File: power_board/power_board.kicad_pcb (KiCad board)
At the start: 2 copper layers, 165.3 x 119.6 mm, 78 parts, among them J1 PROG, J10 M4, J11 5V_1, J12 M5, J13 M6, J14 M7, J15 FAN, J16 Screw_Terminal_01x02, J17 MB_interface, J18 Conn_01x02_Female, J19 12V_1, J2 M1, J20 12V_2, J21 12V_3, J22 12V_4, J23 48V_1, J24 48V_2, J25 48V_3, J26 48V_4, J27 Screw_Terminal_01x02, J3 M2, J4 Conn_01x02_Female, J5 Conn_01x02_Female, J6 Conn_01x01_Male, J7 Conn_01x01_Male, J8 Screw_Terminal_01x02, J9 M3, Q1 2N3906, SW1 SW_Push, U1 ACS758xCB-050B-PFF, U10 MAX31855KASA, U2 ACS758xCB-050B-PFF, U3 MCP2515-EST, U4 MAX31855KASA, U5 MCP2551-I-SN, U6 BTS50085-1TMA, U7 ATmega328P-AU, U8 BTS50085-1TMA, U9 LM2596S-5, Y1 20Mhz, Y2 16Mhz

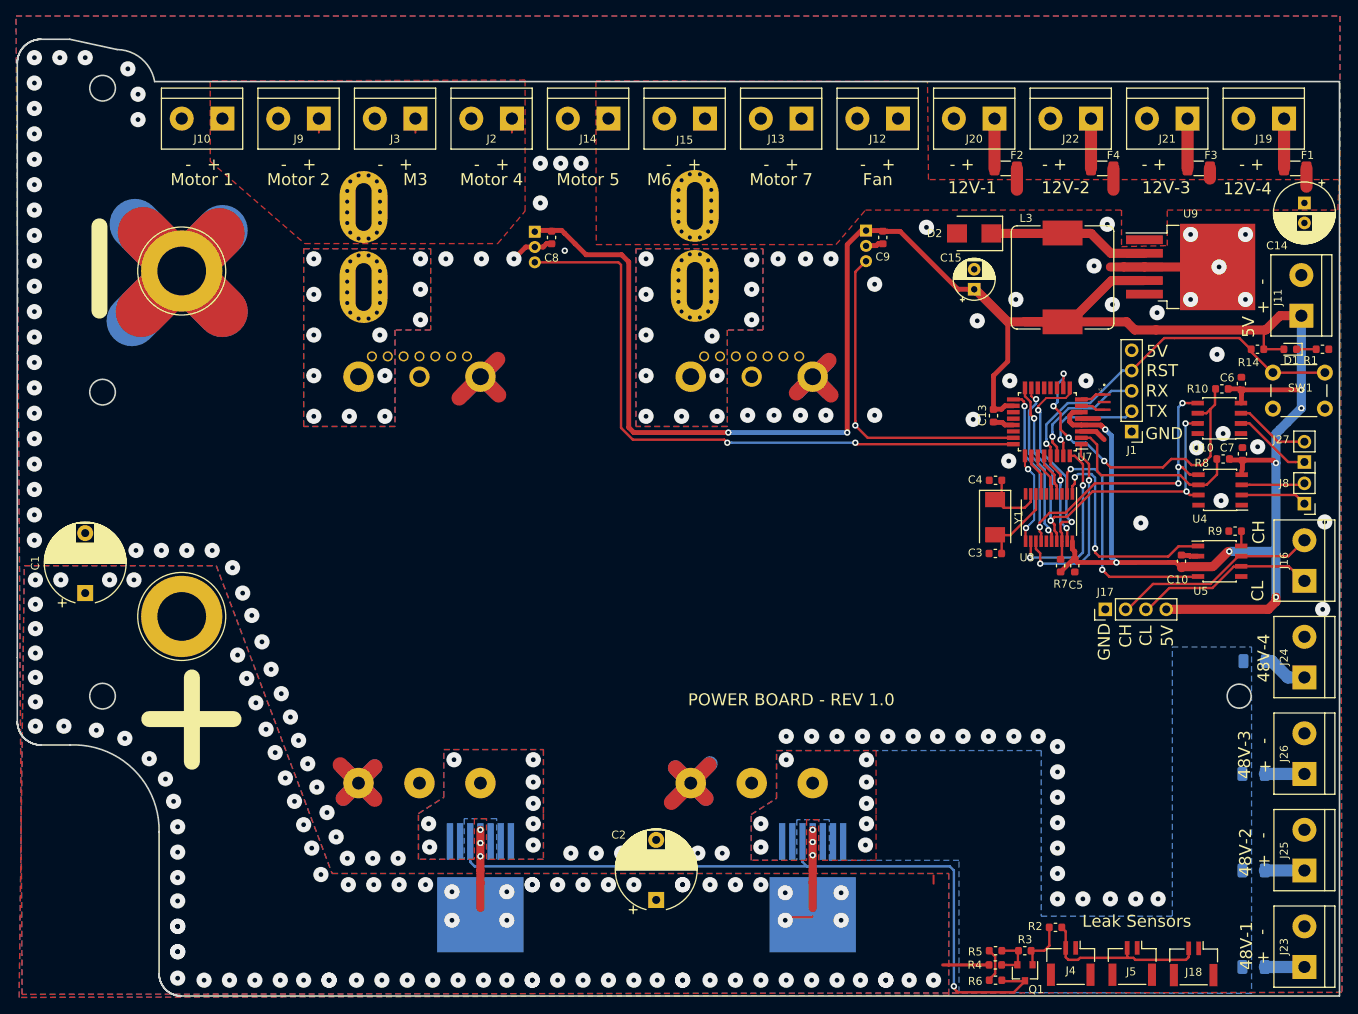
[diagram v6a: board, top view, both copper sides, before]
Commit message: finished re-routing for v_prog diode
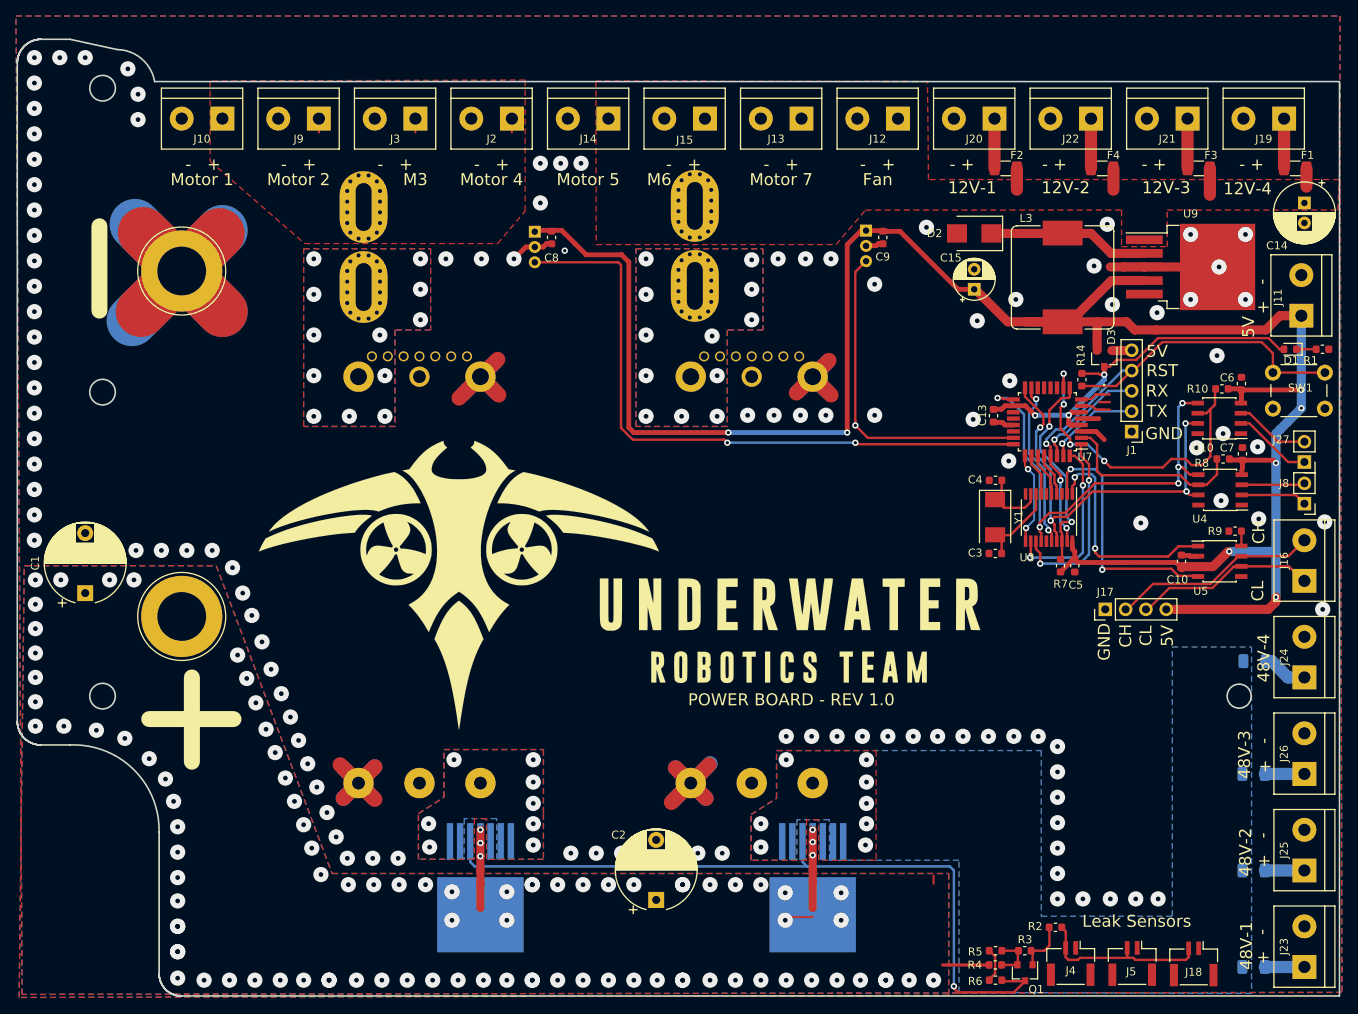
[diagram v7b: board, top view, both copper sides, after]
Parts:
- added D3: D_x2_KCom_AAK, Package_TO_SOT_SMD:SOT-23, F.Cu at (196.6, 71.9)
- added G***: LOGO, logo:logo, F.Cu at (116.1, 99.9)
- added G***: LOGO, title:title, F.Cu at (157.1, 106.2)
- moved R14 22.3 mm to (193.8, 74.5), turned to 270 degrees
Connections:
- C13 pad 1: +5V -> V_MCU
- D1 pad 2: +5V -> V_MCU
- J1 pad 5: +5V -> VPP
- R14 pad 1: +5V -> V_MCU
- U7 pad 18: +5V -> V_MCU
- U7 pad 4: +5V -> V_MCU
- U7 pad 6: +5V -> V_MCU
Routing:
- net V_MCU: track 0.00 -> 49.7 mm, vias 0 -> 3
- net +5V: track 311.0 -> 271.4 mm, vias 9 -> 7
- net RESET: track 57.1 -> 64.0 mm
- net SCK: track 54.8 -> 58.0 mm
- net VPP: track 0.00 -> 2.49 mm
- net +12VA: track 9.11 -> 11.1 mm
- net TX: track 13.7 -> 12.0 mm
- net RX: track 15.8 -> 14.3 mm
- net CAN_CS: track 27.7 -> 26.6 mm
- net MISO: track 51.3 -> 51.8 mm

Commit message: Added 3d models, finished design
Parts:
- U5: value MCP2551-I-SN -> ATA6560,1
- moved R9 7.92 mm to (214.6, 101.2)
- moved G*** 1.40 mm to (114.7, 100.1)
- moved G*** 1.02 mm to (157.0, 105.2)
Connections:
- R9 pad 1: GNDREF -> Net-(R9-Pad1)
- R9 pad 2: Net-(R9-Pad2) -> +5V
- U5 pad 5: Net-(U5-Pad5) -> Net-(R9-Pad1)
- U5 pad 8: Net-(R9-Pad2) -> GNDREF
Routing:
- net Net-(R9-Pad1): track 0.00 -> 2.13 mm
- net +5V: track 271.4 -> 273.4 mm
- net Net-(R9-Pad2): track 1.91 -> 0.00 mm
- net GNDREF: vias 115 -> 114
